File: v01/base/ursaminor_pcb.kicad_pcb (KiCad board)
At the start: 2 copper layers, 298.8 x 122 mm, 145 parts, among them J1 USB_C_Receptacle_USB2.0, J2 I2C-L, J3 I2C-R, J4 AVR-ISP-6, SW1 Reset, U1 ATmega32U4-AU, U2 MCP23017_SO, U3 PRTR5V0U2X, U4 HOLE, U4 PRTR5V0U2X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

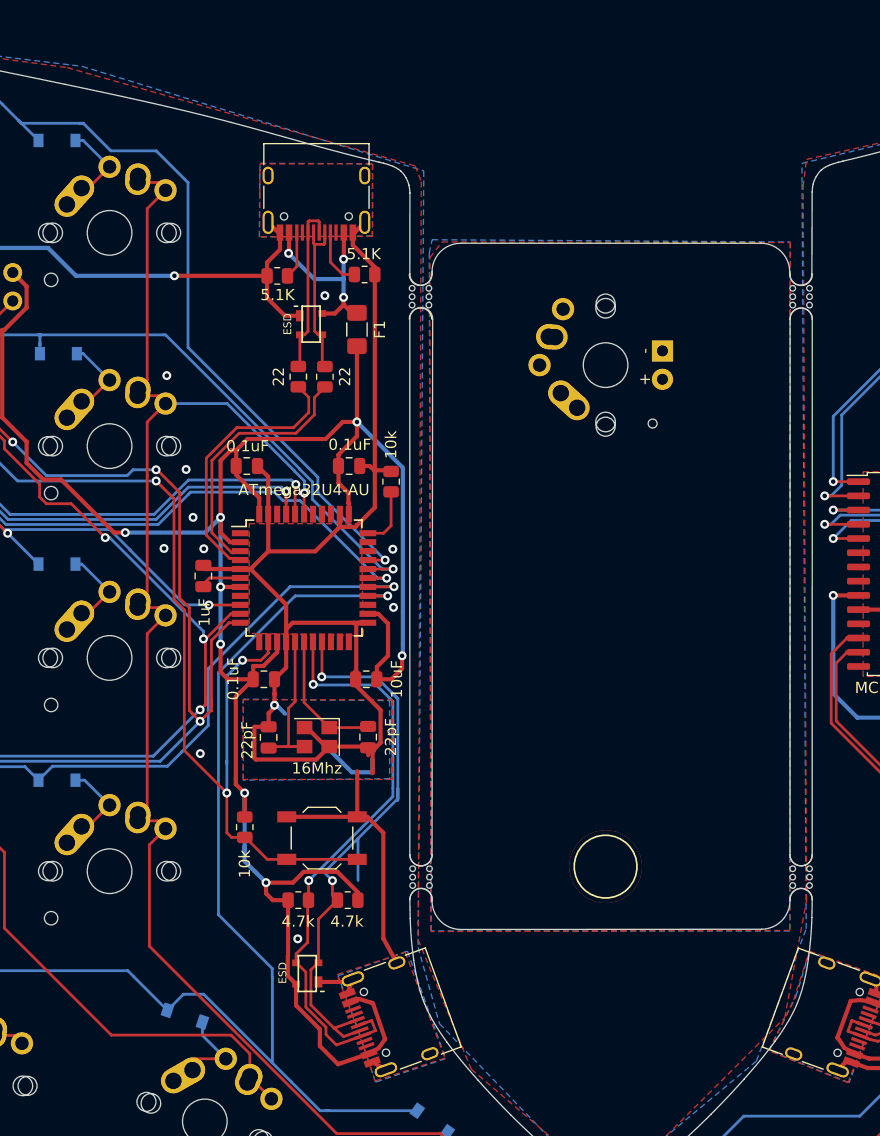
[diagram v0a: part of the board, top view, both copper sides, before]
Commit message: Use 5mm mousebites instead
The reveiwers at JLCPCB requested wider mousebites as 2mm
ones are 'too small'.
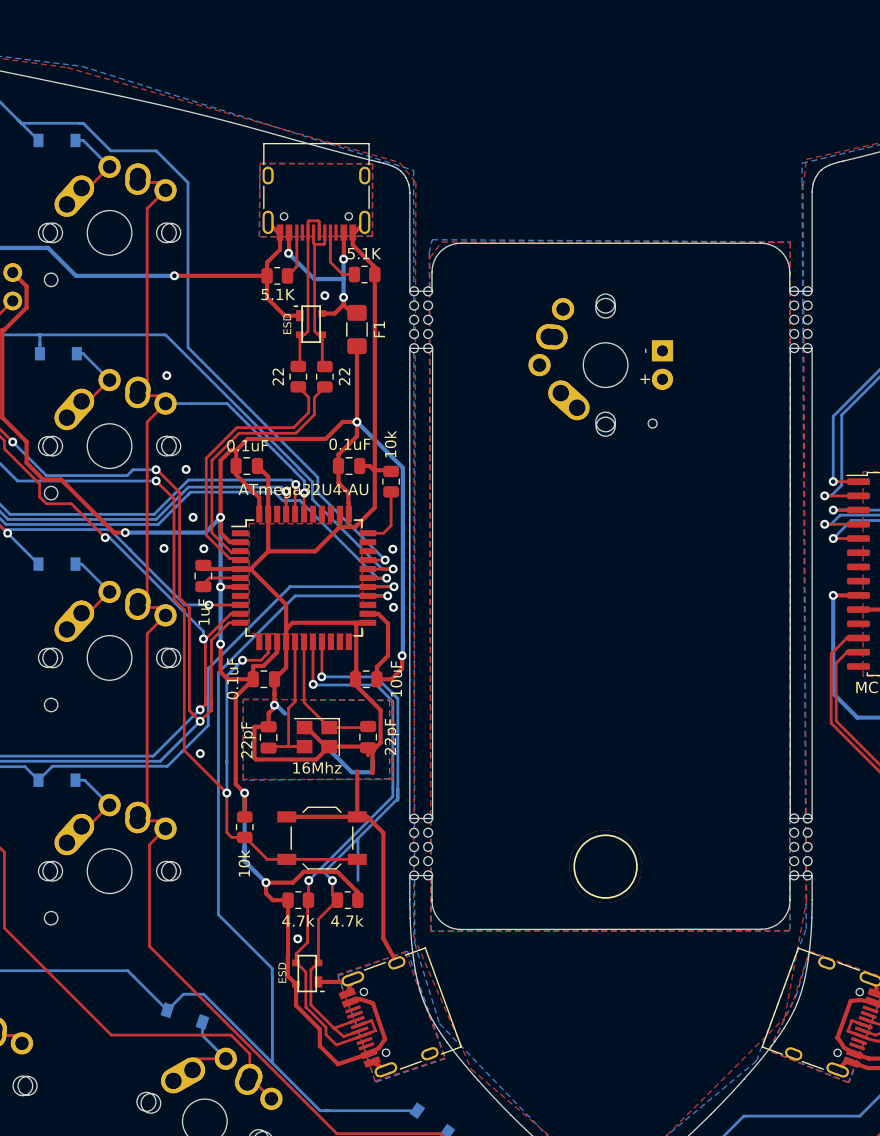
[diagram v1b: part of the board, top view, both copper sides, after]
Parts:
- removed mouse-bite-2mm-slot (x4): VAL**, Panelization:mouse-bite-2mm-slot
- added REF**: breakaway-mousebites, Keebio-Parts:breakaway-mousebites, F.Cu at (193.8, 52.8)
- added REF**: breakaway-mousebites, Keebio-Parts:breakaway-mousebites, F.Cu at (192.6, 52.8)
- added REF**: breakaway-mousebites, Keebio-Parts:breakaway-mousebites, F.Cu at (193.8, 99.9)
- added REF**: breakaway-mousebites, Keebio-Parts:breakaway-mousebites, F.Cu at (192.6, 99.9)
- added REF**: breakaway-mousebites, Keebio-Parts:breakaway-mousebites, F.Cu at (158.7, 100.0)
- added REF**: breakaway-mousebites, Keebio-Parts:breakaway-mousebites, F.Cu at (159.9, 99.9)
- added REF**: breakaway-mousebites, Keebio-Parts:breakaway-mousebites, F.Cu at (159.9, 52.9)
- added REF**: breakaway-mousebites, Keebio-Parts:breakaway-mousebites, F.Cu at (158.7, 52.9)
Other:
- outline, holes or cut-outs redrawn

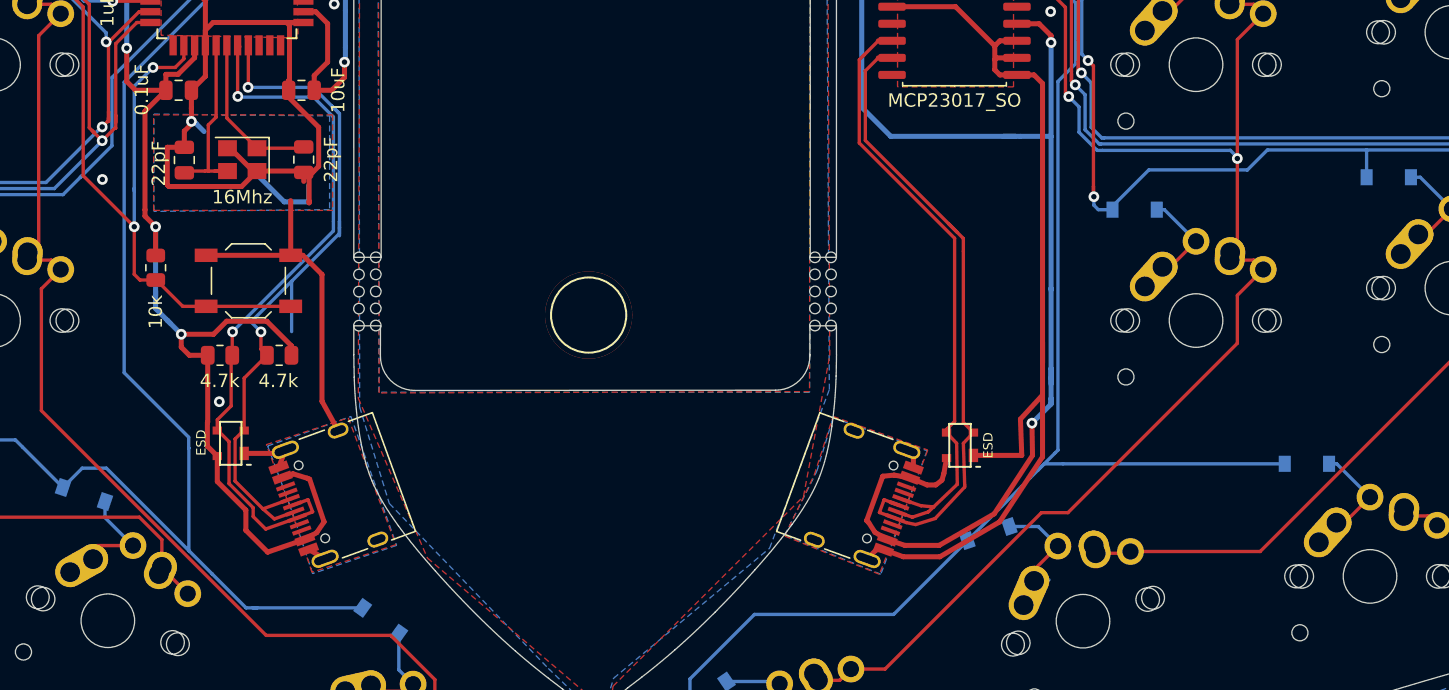
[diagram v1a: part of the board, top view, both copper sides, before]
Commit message: Remove stray trace and fix fill zones
Found some problems in the printed boards.
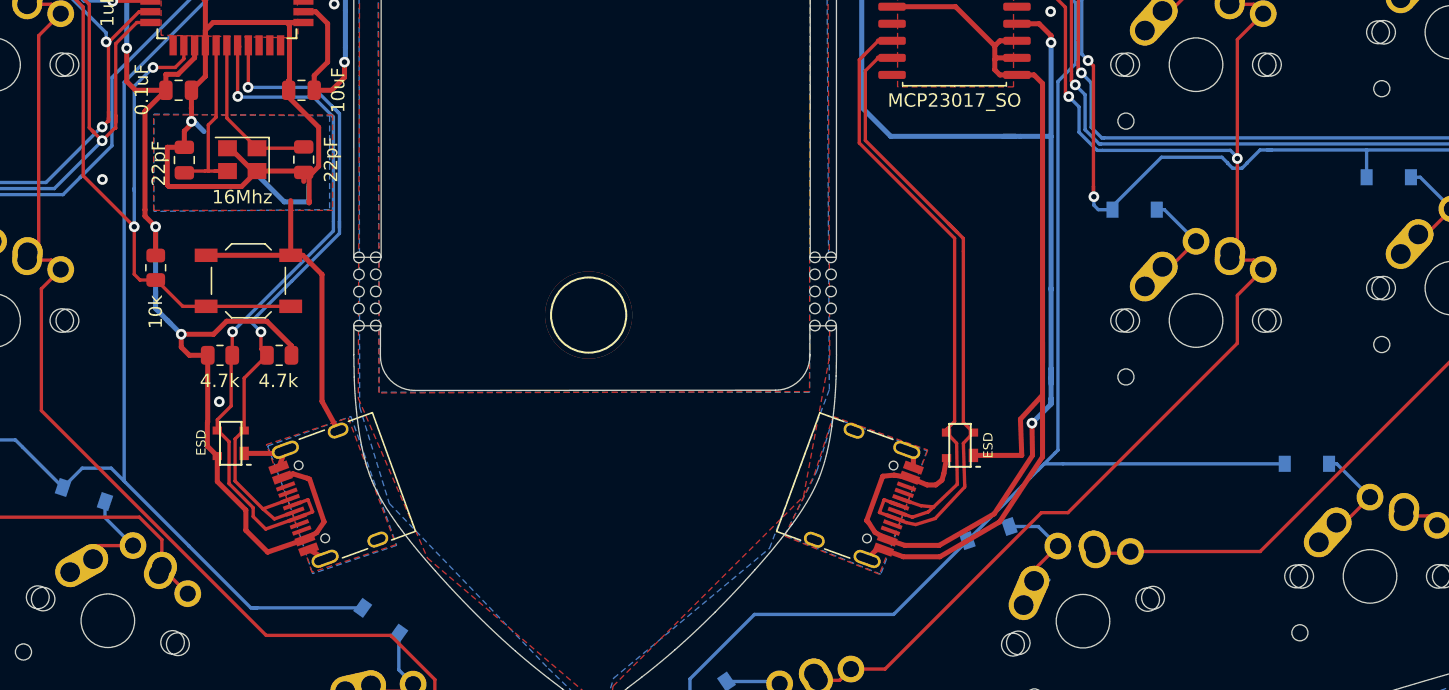
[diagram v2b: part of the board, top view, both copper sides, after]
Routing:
- net Row4-L: track 111.4 -> 104.3 mm
- net SDA-L: track 55.6 -> 51.3 mm
- net Row3-R: track 150.6 -> 151.6 mm
